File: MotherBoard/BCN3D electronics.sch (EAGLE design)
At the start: 195 parts, among them IC1 LM358D, IC2 FT232RL, IC3 LM311D, K1 G5L, Q1 MOSFET-NSOIC8, Q2 MOSFET-NSOIC8, Q3 MOSFET-NSOIC8, Q4 MMBT2222A, Q5 MMBT2222A, Q9 MMBT2222A, U1 INA169, X0 FFC_15V_90G_1MM, X1 FFC_15V_90G_1MM, Y0 FFC_15V_90G_1MM

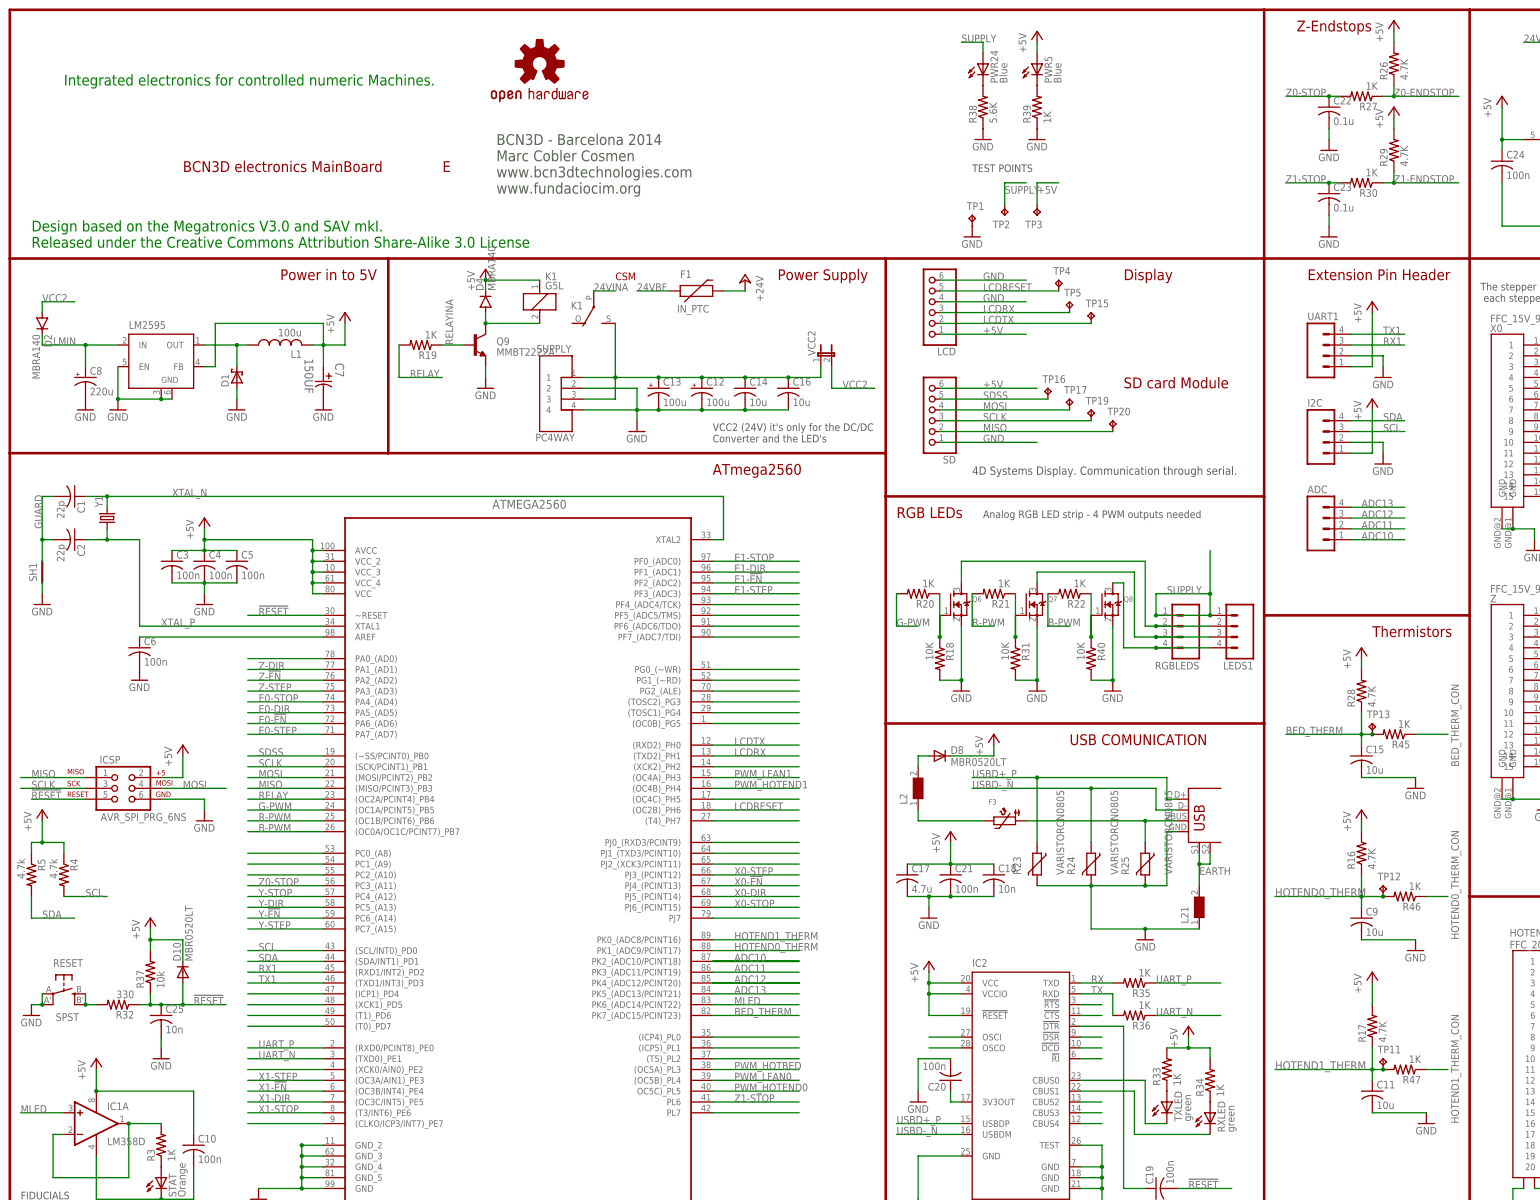
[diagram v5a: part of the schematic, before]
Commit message: Fixed thermistor series resistors
Added new license info and WEEE/FCC/CE Logo.
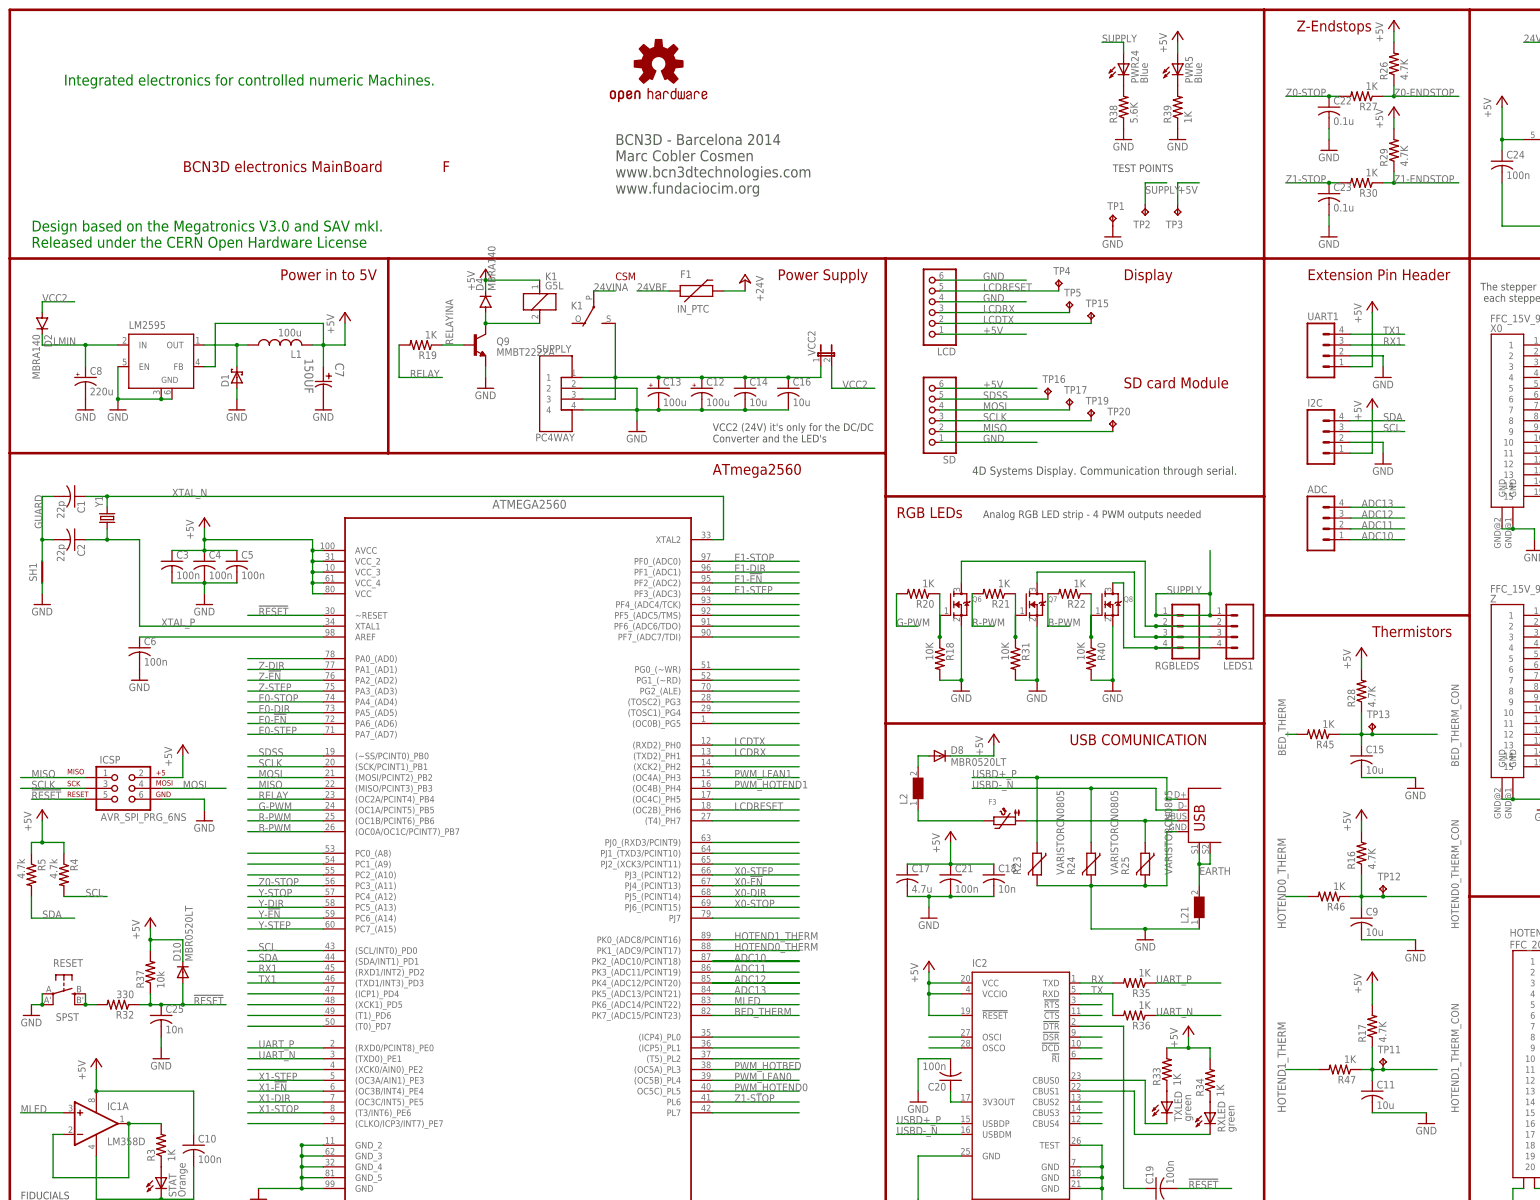
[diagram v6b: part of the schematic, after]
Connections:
- net BED_THERM: no longer C15.1, R28.1, TP13.TP
- net BED_THERM_CON: now also C15.1, R28.1, TP13.TP
- net HOTEND0_THERM: no longer C9.1, R16.1, TP12.TP
- net HOTEND0_THERM_CON: now also C9.1, R16.1, TP12.TP
- net HOTEND1_THERM: no longer C11.1, R17.1, TP11.TP
- net HOTEND1_THERM_CON: now also C11.1, R17.1, TP11.TP
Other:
- note added: "Design based on the Megatronics V3.0 and SAV mkI. Released under the CERN Open Hardware License"
- note added: "F"
- note removed: "Design based on the Megatronics V3.0 and SAV mkI. Released under the Creative Commons Attribution Share-Alike 3.0 License"
- note removed: "E"
- moved on the sheet: PWR24, PWR5, R38, R39, R45, R46, R47, TP1, TP2, TP3
